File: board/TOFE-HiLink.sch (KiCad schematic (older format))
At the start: 11 parts, among them U1 TOFE-8X, U7 24AA01/24LC01B

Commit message: schematic: Removing old parts
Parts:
- removed J? (x3): DISPLAY_PORT, symbol DISPLAY_PORT
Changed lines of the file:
@@
 Entry Wire Line
 	6720 5700 6820 5800
-$Comp
-L DISPLAY_PORT J?
-U 1 1 5631E449
-P 8640 2930
-F 0 "J?" H 8040 4030 60  0000 C CNN
-F 1 "DISPLAY_PORT" V 8790 2930 60  0000 C CNN
-F 2 "" H 8590 2930 60  0000 C CNN
-F 3 "" H 8590 2930 60  0000 C CNN
-	1    8640 2930
-	1    0    0    -1
-$EndComp
-$Comp
-L DISPLAY_PORT J?
-U 1 1 5631EC74
-P 1080 6430
-F 0 "J?" H 480 7530 60  0000 C CNN
-F 1 "DISPLAY_PORT" V 1230 6430 60  0000 C CNN
-F 2 "" H 1030 6430 60  0000 C CNN
-F 3 "" H 1030 6430 60  0000 C CNN
-	1    1080 6430
-	-1   0    0    -1
-$EndComp
-$Comp
-L DISPLAY_PORT J?
-U 1 1 5631E90F
-P 1300 2970
-F 0 "J?" H 700 4070 60  0000 C CNN
-F 1 "DISPLAY_PORT" V 1450 2970 60  0000 C CNN
-F 2 "" H 1250 2970 60  0000 C CNN
-F 3 "" H 1250 2970 60  0000 C CNN
-	1    1300 2970
-	-1   0    0    -1
-$EndComp
 $EndSCHEMATC

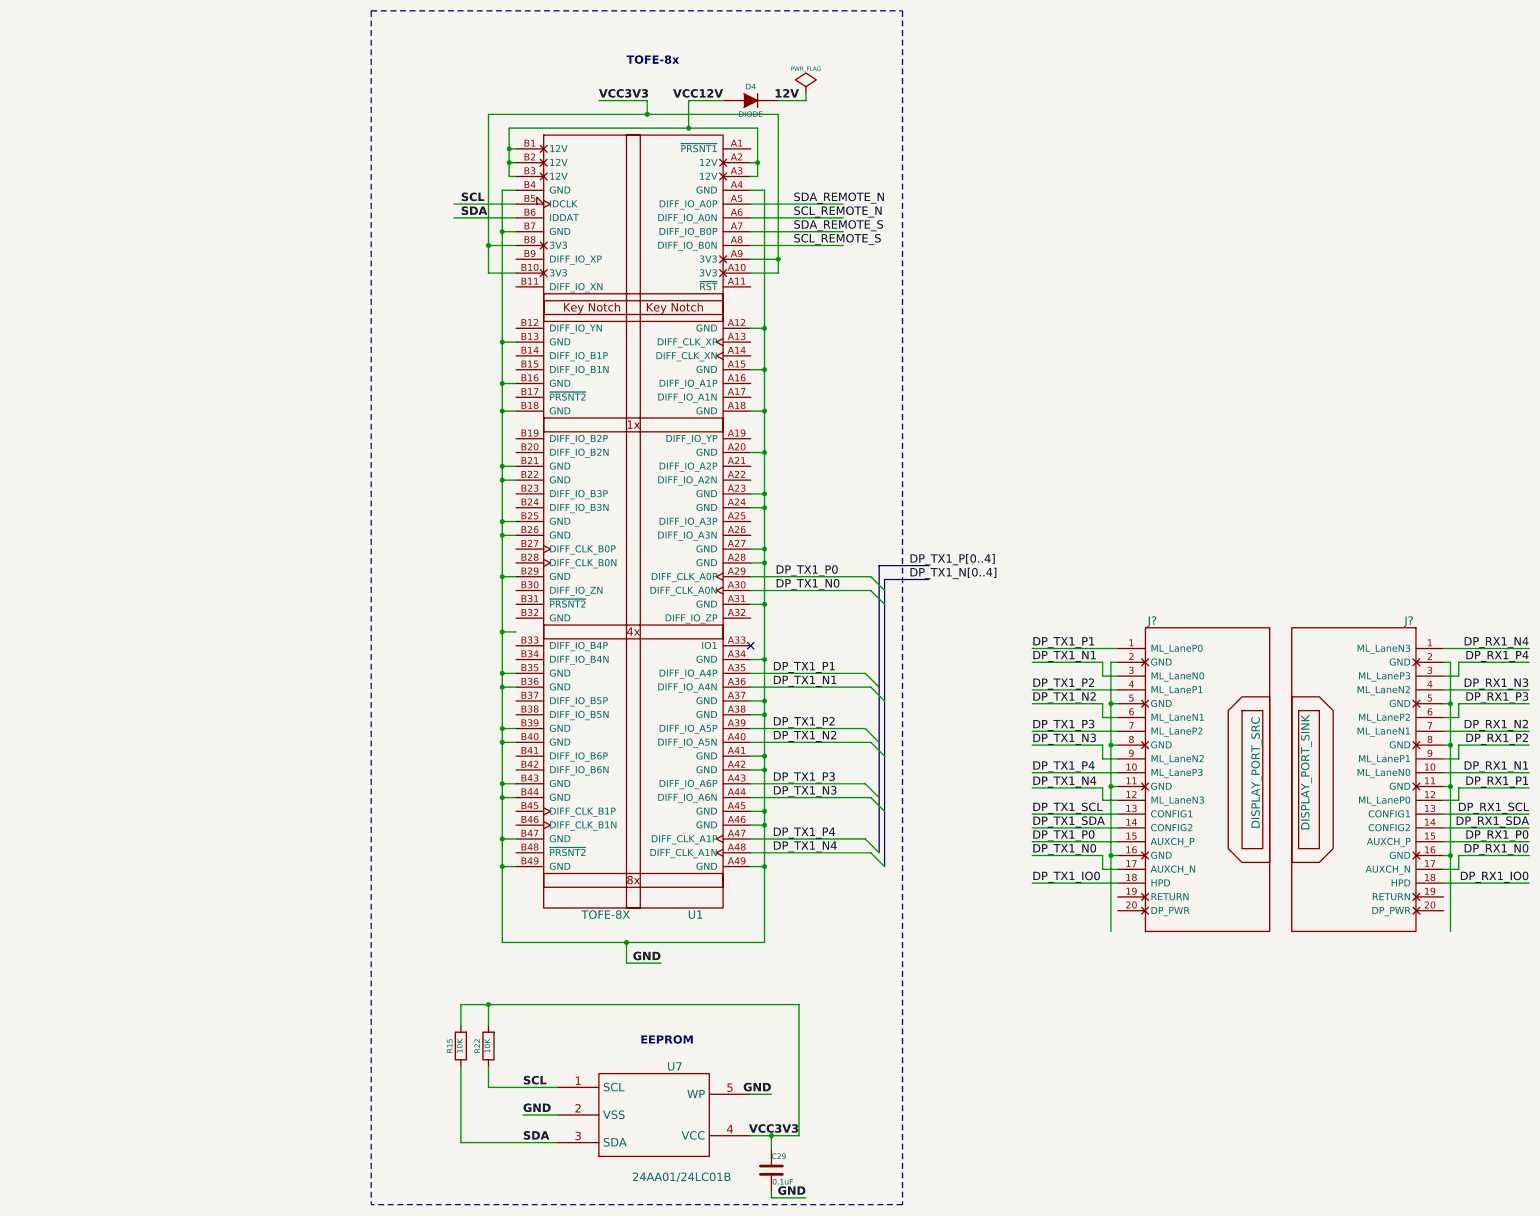
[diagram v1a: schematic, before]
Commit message: Mostly done the TOFE side.
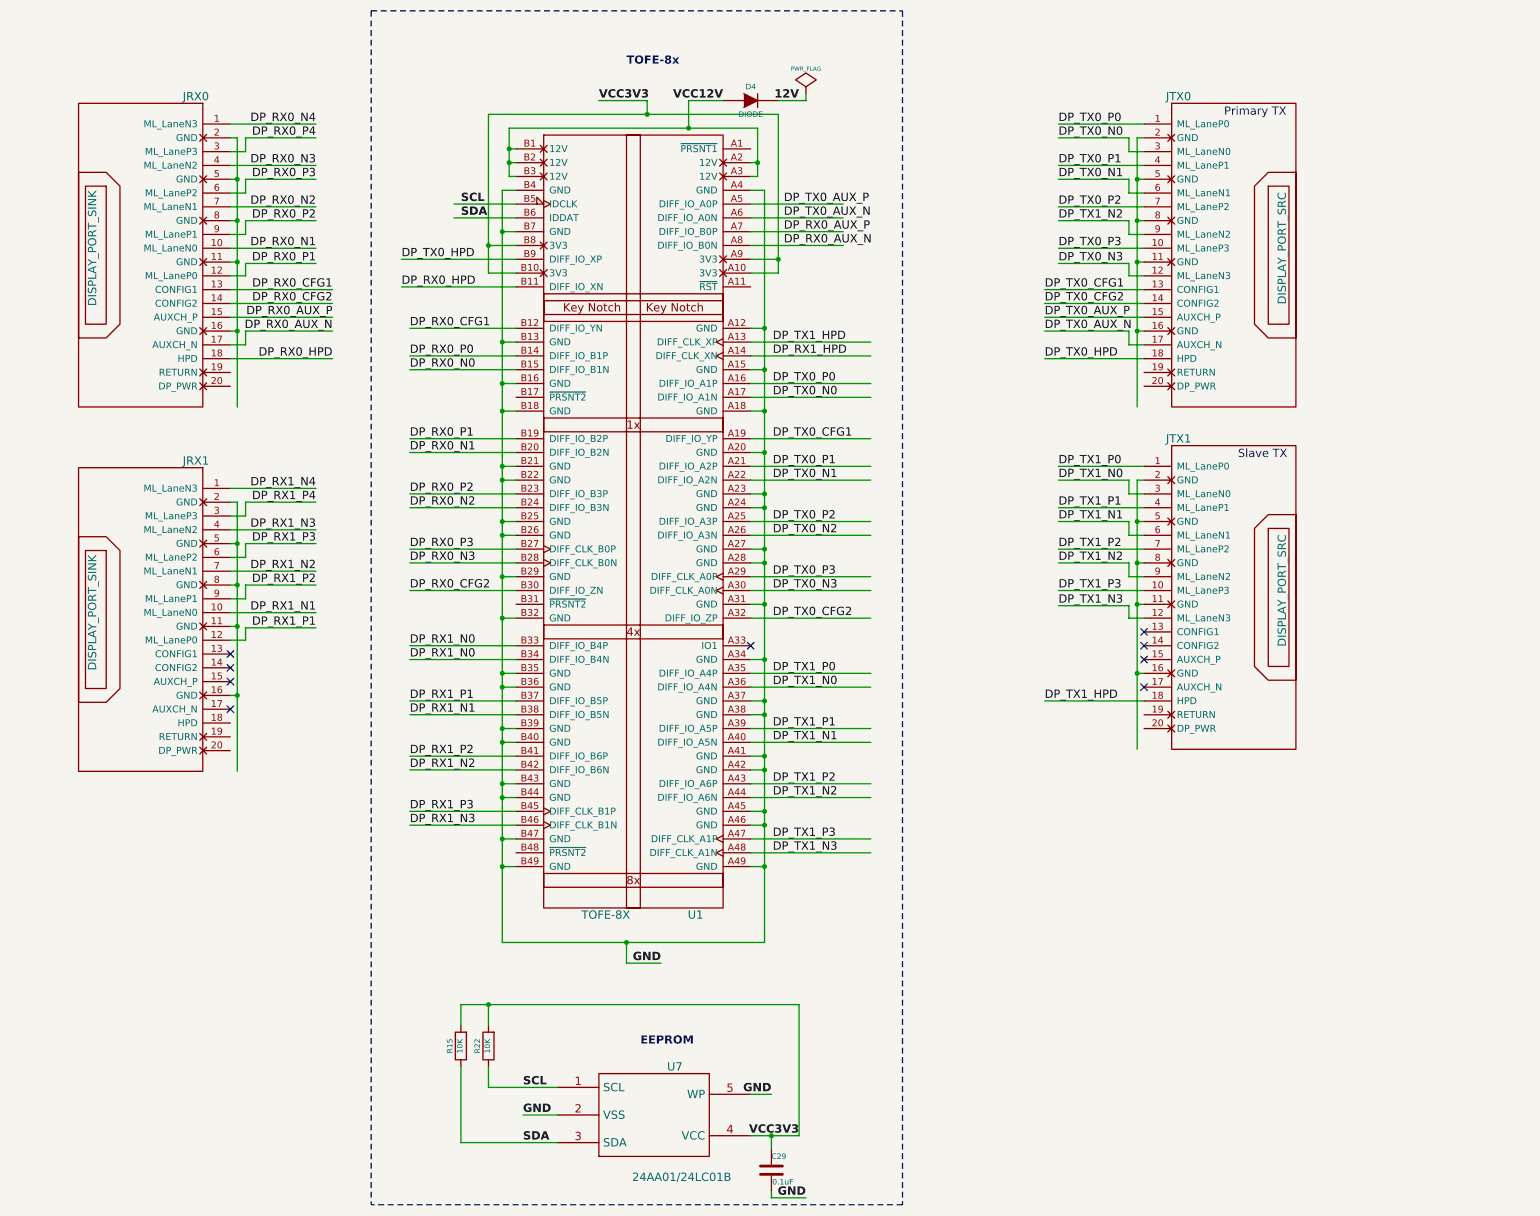
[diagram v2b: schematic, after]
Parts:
- added JRX1: DISPLAY_PORT_SINK, symbol DISPLAY_PORT_SINK
- added JTX1: DISPLAY_PORT_SRC, symbol DISPLAY_PORT_SRC
- gave numbers to parts that had none: 2
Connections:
- net labels added: DP_RX0_AUX_N, DP_RX0_AUX_P, DP_RX0_CFG1, DP_RX0_CFG2, DP_RX0_HPD, DP_RX0_N0, DP_RX0_N1, DP_RX0_N2, DP_RX0_N3, DP_RX0_N4, DP_RX0_P0, DP_RX0_P1, DP_RX0_P2, DP_RX0_P3, DP_RX0_P4, DP_RX1_HPD, DP_TX0_AUX_N, DP_TX0_AUX_P, DP_TX0_CFG1, DP_TX0_CFG2, DP_TX0_HPD, DP_TX0_N0, DP_TX0_N1, DP_TX0_N2, DP_TX0_N3, DP_TX0_P0, DP_TX0_P1, DP_TX0_P2, DP_TX0_P3, DP_TX1_HPD
- net labels removed: DP_RX1_IO0, DP_RX1_P0, DP_RX1_SCL, DP_RX1_SDA, DP_TX1_IO0, DP_TX1_N4, DP_TX1_N[0..4], DP_TX1_P4, DP_TX1_P[0..4], DP_TX1_SCL, DP_TX1_SDA, SCL_REMOTE_N, SCL_REMOTE_S, SDA_REMOTE_N, SDA_REMOTE_S
- wire segments 204 -> 287
- no-connect marks 1 -> 9
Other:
- note added: "Primary TX"
- note added: "Slave TX"
- moved on the sheet: JRX0, JTX0
